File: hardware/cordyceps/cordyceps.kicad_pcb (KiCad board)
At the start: 4 copper layers, 22.1 x 29.9 mm, 23 parts, among them J1 KH-1.27PH180-2X5P-L7.2-SMT, SW1 TS-1187A-B-A-B, U1 nRF52833-QDxx, X1 32Mhz crystal, X2 32.768kHz crystal

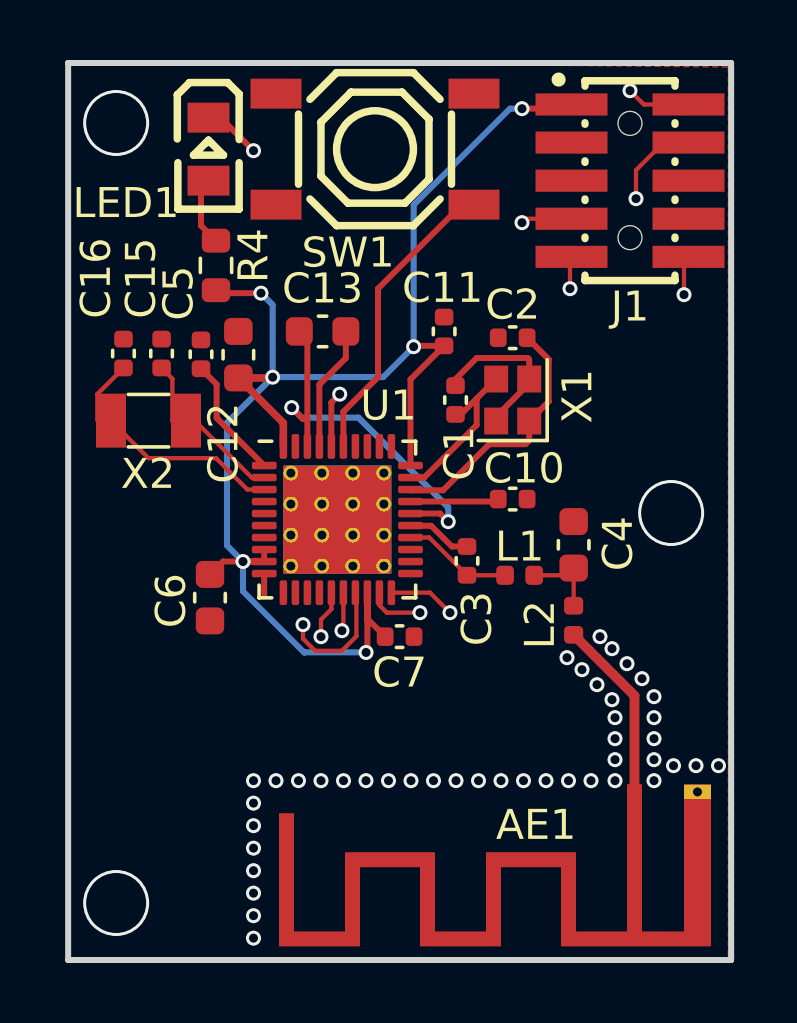
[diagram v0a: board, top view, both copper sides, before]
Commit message: Remove some redundant tracks
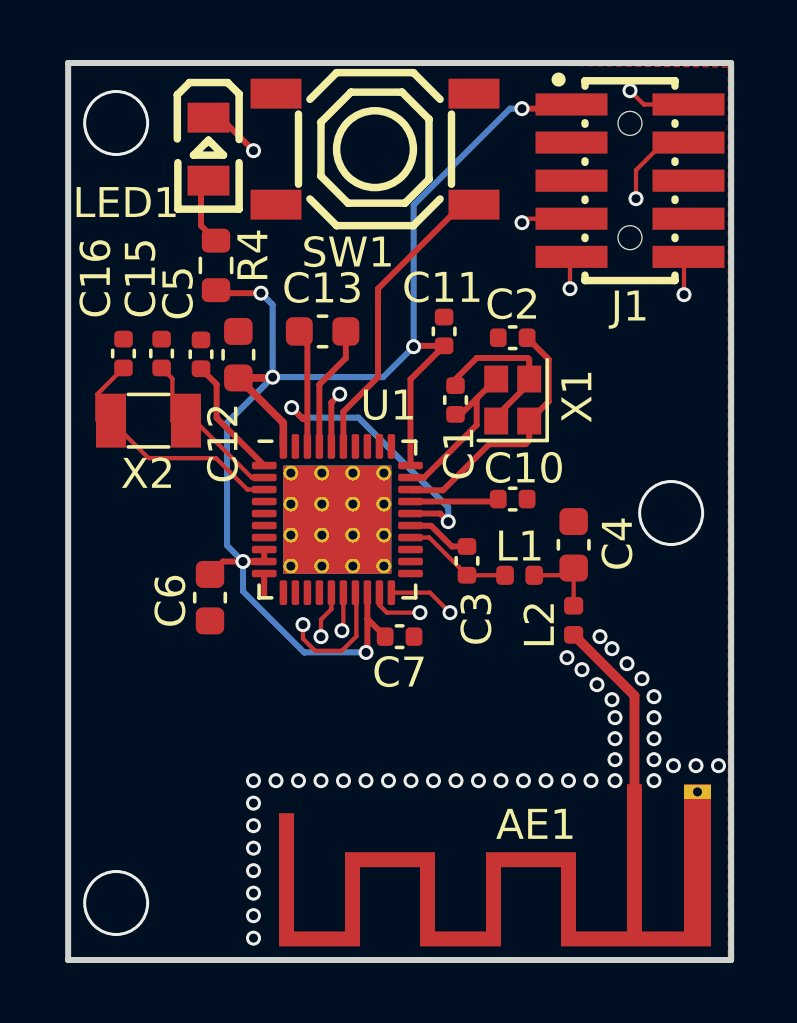
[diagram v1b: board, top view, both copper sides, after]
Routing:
- net VDD: track 51.2 -> 49.4 mm
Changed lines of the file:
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@@
-	)
-	(segment
-		(start 123.045779 90.675778)
-		(end 123.045779 89.733479)
-		(width 0.2)
-		(layer "F.Cu")
-		(net 8)
-	)
-	(segment
-		(start 123.045779 90.605779)
-		(end 123.045779 89.733479)
-		(width 0.2)
-		(layer "F.Cu")
-		(net 8)
 	)
 	(segment

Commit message: Add 2 MOSFETs to be able to turn things on and off
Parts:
- added D1: 1N5819WS, easyeda2kicad:SOD-323_L1.8-W1.3-LS2.5-RD, F.Cu at (117.8, 97.8)
- added Q1: 2N7002, Package_TO_SOT_SMD:SOT-23, F.Cu at (122.5, 93.8)
- added Q2: IRML6401, Package_TO_SOT_SMD:SOT-23, F.Cu at (118.5, 93.8)
- added R1: 10k, Resistor_SMD:R_0402_1005Metric, F.Cu at (125.5, 93.2)
- added R2: 10k, Resistor_SMD:R_0402_1005Metric, F.Cu at (125.5, 94.3)
- moved C7 1.17 mm to (125.2, 91.5)
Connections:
- U1 pad 14: unconnected-(U1-P0.15-Pad14) -> Net-(Q1-G)
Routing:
- net VDD: track 49.4 -> 61.5 mm, vias 6 -> 7
- net Net-(Q1-G): track 0.00 -> 8.00 mm
- net Net-(Q1-D): track 0.00 -> 6.22 mm
- net /V_OUT: track 0.00 -> 2.39 mm
- net GND: vias 43 -> 44

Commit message: Add required connectors
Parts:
- added J2: Rothult_Debug_Header, Connector_PinHeader_1.27mm:PinHeader_1x06_P1.27mm_Vertical, F.Cu at (114.7, 93.7)
- added J3: Conn_01x03_Pin, Connector_PinHeader_2.54mm:PinHeader_1x03_P2.54mm_Vertical, F.Cu at (133.6, 90.7)
- added R3: 10k, Resistor_SMD:R_0402_1005Metric, F.Cu at (117.8, 86.7)
- added R5: 10k, Resistor_SMD:R_0402_1005Metric, F.Cu at (116.8, 86.7)
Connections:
- net /V_OUT renamed Net-(D1-C)
- U1 pad 6: unconnected-(U1-P1.09-Pad6) -> /ROTHULT_TX
- U1 pad 7: unconnected-(U1-P0.011-Pad7) -> /ROTHULT_RX
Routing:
- net VDD: track 61.5 -> 82.7 mm, vias 7 -> 8
- net Net-(D1-C): track 2.39 -> 21.4 mm, vias 0 -> 1
- net /ROTHULT_RX: track 0.00 -> 5.76 mm
- net /ROTHULT_TX: track 0.00 -> 5.48 mm
- net GND: vias 44 -> 45
- net (no net): vias 3 -> 2
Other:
- board text added: "CLK"
- board text added: "GND"
- board text added: "IO"
- board text added: "V_IN"
- board text added: "V_OUT"

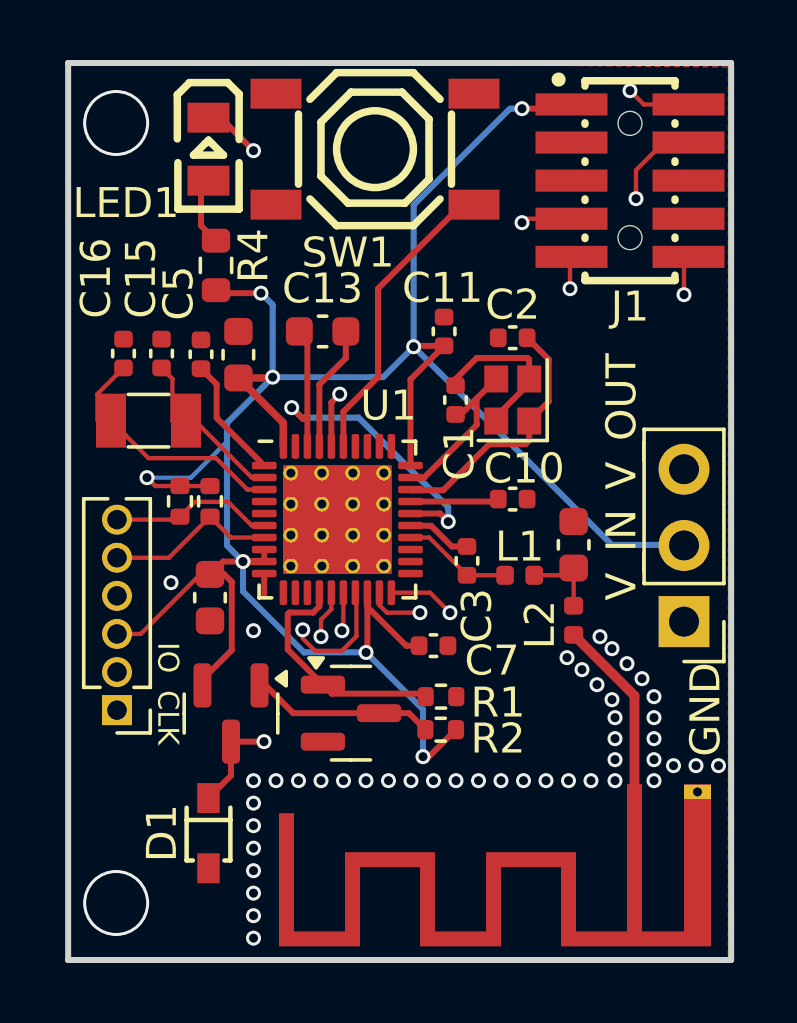
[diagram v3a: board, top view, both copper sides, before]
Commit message: Add some GND vias
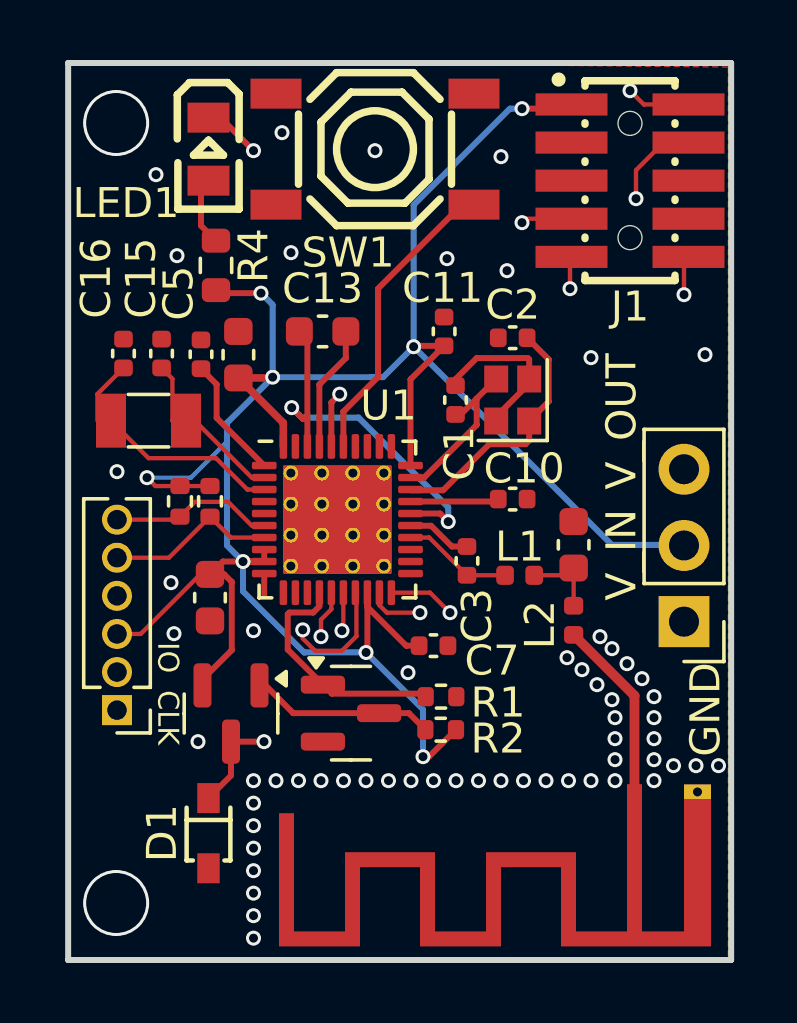
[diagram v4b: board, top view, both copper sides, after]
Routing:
- net GND: vias 45 -> 59
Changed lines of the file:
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@@
 		)
 		(property "Value" "Rothult_Debug_Header"
-			(at 0 8.045 360)
+			(at 0 8.045 0)
 			(layer "F.Fab")
 			(effects
@@
 		(tags "Through hole pin header THT 1x03 2.54mm single row")
 		(property "Reference" "J3"
-			(at 0.1 -2.5 360)
+			(at 0.1 -2.5 0)
 			(layer "F.SilkS")
 			(hide yes)
@@
 		)
 		(property "Value" "Conn_01x03_Pin"
-			(at 0 7.41 360)
+			(at 0 7.41 0)
 			(layer "F.Fab")
 			(effects
@@
 	)
 	(via
+		(at 116 75.8)
+		(size 0.5)
+		(drill 0.3)
+		(layers "F.Cu" "B.Cu")
+		(free yes)
+		(net 3)
+	)
+	(via
 		(at 129 96)
 		(size 0.5)
@@
 	)
 	(via
+		(at 127.5 75.2)
+		(size 0.5)
+		(drill 0.3)
+		(layers "F.Cu" "B.Cu")
+		(free yes)
+		(net 3)
+	)
+	(via
 		(at 131.3 96)
 		(size 0.5)
@@
 	)
 	(via
+		(at 123.3 75)
+		(size 0.5)
+		(drill 0.3)
+		(layers "F.Cu" "B.Cu")
+		(free yes)
+		(net 3)
+	)
+	(via
 		(at 123 96)
 		(size 0.5)
@@
 	)
 	(via
+		(at 134.3 81.8)
+		(size 0.5)
+		(drill 0.3)
+		(layers "F.Cu" "B.Cu")
+		(free yes)
+		(net 3)
+	)
+	(via
 		(at 125.25 96)
 		(size 0.5)
@@
 	)
 	(via
+		(at 124.4 92.4)
+		(size 0.5)
+		(drill 0.3)
+		(layers "F.Cu" "B.Cu")
+		(free yes)
+		(net 3)
+	)
+	(via
 		(at 132.6 95.3)
 		(size 0.5)
@@
 	)
 	(via
+		(at 117.4 94.7)
+		(size 0.5)
+		(drill 0.3)
+		(layers "F.Cu" "B.Cu")
+		(free yes)
+		(net 3)
+	)
+	(via
 		(at 119.25 99)
 		(size 0.5)
@@
 	)
 	(via
+		(at 120.5 78.4)
+		(size 0.5)
+		(drill 0.3)
+		(layers "F.Cu" "B.Cu")
+		(free yes)
+		(net 3)
+	)
+	(via
 		(at 134.75 95.5)
 		(size 0.5)
@@
 	)
 	(via
+		(at 114.7 85.7)
+		(size 0.5)
+		(drill 0.3)
+		(layers "F.Cu" "B.Cu")
+		(free yes)
+		(net 3)
+	)
+	(via
+		(at 120.2 74.4)
+		(size 0.5)
+		(drill 0.3)
+		(layers "F.Cu" "B.Cu")
+		(free yes)
+		(net 3)
+	)
+	(via
 		(at 132.2 92.6)
 		(size 0.5)
@@
 	)
 	(via
+		(at 116.6 91.1)
+		(size 0.5)
+		(drill 0.3)
+		(layers "F.Cu" "B.Cu")
+		(free yes)
+		(net 3)
+	)
+	(via
 		(at 131.3 95.3)
 		(size 0.5)
@@
 	)
 	(via
+		(at 127.7 79)
+		(size 0.5)
+		(drill 0.3)
+		(layers "F.Cu" "B.Cu")
+		(free yes)
+		(net 3)
+	)
+	(via
 		(at 120.75 96)
 		(size 0.5)
@@
 	)
 	(via
+		(at 130.5 81.9)
+		(size 0.5)
+		(drill 0.3)
+		(layers "F.Cu" "B.Cu")
+		(free yes)
+		(net 3)
+	)
+	(via
 		(at 130.2 92.3)
 		(size 0.5)
@@
 		(size 0.5)
 		(drill 0.3)
+		(layers "F.Cu" "B.Cu")
+		(free yes)
+		(net 3)
+	)
+	(via
+		(at 125.7 78.6)
+		(size 0.5)
+		(drill 0.3)
+		(layers "F.Cu" "B.Cu")
+		(free yes)
+		(net 3)
+	)
+	(via
+		(at 116.7 78.5)
+		(size 0.5)
+		(drill 0.3)

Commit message: Fix the small fuckup with the UART RX/TX on cordyceps board
Oops, I did it again!
Luckily, we can just reassign those as nRF chips allow to use any pin as RX/TX.
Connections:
- J1 pad 7: /DBG_TX -> /DBG_RX
- J1 pad 9: /DBG_RX -> /DBG_TX
- U1 pad 15: /DBG_RX -> /DBG_TX
- U1 pad 17: /DBG_TX -> /DBG_RX
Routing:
- net /DBG_TX: track 23.4 -> 18.8 mm
- net /DBG_RX: track 18.8 -> 23.4 mm
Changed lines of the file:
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@@
 			(layers "F.Cu" "F.Paste" "F.Mask")
 			(roundrect_rratio 0.25)
-			(net 24 "/DBG_RX")
+			(net 37 "/DBG_TX")
 			(pinfunction "P0.17")
 			(pintype "bidirectional")
@@
 			(layers "F.Cu" "F.Paste" "F.Mask")
 			(roundrect_rratio 0.25)
-			(net 37 "/DBG_TX")
+			(net 24 "/DBG_RX")
 			(pinfunction "P0.20")
 			(pintype "bidirectional")
@@
 			(size 0.74 2.4)
 			(layers "F.Cu" "F.Paste" "F.Mask")
-			(net 37 "/DBG_TX")
+			(net 24 "/DBG_RX")
 			(pinfunction "7")
 			(pintype "unspecified")
@@
 			(size 0.74 2.4)
 			(layers "F.Cu" "F.Paste" "F.Mask")
-			(net 24 "/DBG_RX")
+			(net 37 "/DBG_TX")
 			(pinfunction "9")
 			(pintype "unspecified")
@@
 	)
 	(segment
-		(start 129.8 79.6)
-		(end 129.8 78.59)
+		(start 122.195716 91.6725)
+		(end 122.68045 91.187766)
 		(width 0.145)
 		(layer "F.Cu")
@@
 	)
 	(segment
-		(start 129.8 78.59)
-		(end 129.85 78.54)
+		(start 122.68045 89.76815)
+		(end 122.645779 89.733479)
 		(width 0.145)
 		(layer "F.Cu")
@@
 	)
 	(segment
-		(start 121.5 91.2)
-		(end 121.5 90.631784)
+		(start 121.304284 91.6725)
+		(end 122.195716 91.6725)
 		(width 0.145)
 		(layer "F.Cu")
@@
 	)
 	(segment
-		(start 121.845779 90.286005)
-		(end 121.845779 89.733479)
+		(start 128.2 77.4)
+		(end 128.33 77.27)
 		(width 0.145)
 		(layer "F.Cu")
@@
 	)
 	(segment
-		(start 121.5 90.631784)
-		(end 121.845779 90.286005)
+		(start 120.89092 91.259136)
+		(end 121.304284 91.6725)
+		(width 0.145)
+		(layer "F.Cu")
+		(net 24)
+	)
+	(segment
+		(start 120.89092 90.973013)
+		(end 120.89092 91.259136)
+		(width 0.145)
+		(layer "F.Cu")
+		(net 24)
+	)
+	(segment
+		(start 128.33 77.27)
+		(end 129.85 77.27)
+		(width 0.145)
+		(layer "F.Cu")
+		(net 24)
+	)
+	(segment
+		(start 122.68045 91.187766)
+		(end 122.68045 89.76815)
 		(width 0.145)
 		(layer "F.Cu")
@@
 	)
 	(via
-		(at 121.5 91.2)
+		(at 120.89092 90.973013)
 		(size 0.5)
 		(drill 0.3)
@@
 	)
 	(via
-		(at 129.8 79.6)
+		(at 128.2 77.4)
 		(size 0.5)
 		(drill 0.3)
@@
 	)
 	(segment
-		(start 121.5 91.031784)
-		(end 122.604284 89.9275)
+		(start 120.89092 90.973013)
+		(end 120.958771 90.973013)
 		(width 0.145)
 		(layer "In2.Cu")
@@
 	)
 	(segment
-		(start 129.8 84.6)
-		(end 129.8 79.6)
+		(start 125.060279 80.539721)
+		(end 128.2 77.4)
 		(width 0.145)
 		(layer "In2.Cu")
@@
 	)
 	(segment
-		(start 124.4725 89.9275)
-		(end 129.8 84.6)
+		(start 124.2 89.6)
+		(end 125.060279 88.739721)
 		(width 0.145)
 		(layer "In2.Cu")
@@
 	)
 	(segment
-		(start 122.604284 89.9275)
-		(end 124.4725 89.9275)
+		(start 125.060279 88.739721)
+		(end 125.060279 80.539721)
 		(width 0.145)
 		(layer "In2.Cu")
@@
 	)
 	(segment
-		(start 121.5 91.2)
-		(end 121.5 91.031784)
+		(start 120.958771 90.973013)
+		(end 122.331784 89.6)
 		(width 0.145)
 		(layer "In2.Cu")
@@
 	)
 	(segment
-		(start 122.195716 91.6725)
-		(end 122.68045 91.187766)
-		(width 0.145)
-		(layer "F.Cu")
-		(net 37)
-	)
-	(segment
-		(start 122.68045 89.76815)
-		(end 122.645779 89.733479)
-		(width 0.145)
-		(layer "F.Cu")
-		(net 37)
-	)
-	(segment
-		(start 121.304284 91.6725)
-		(end 122.195716 91.6725)
+		(start 122.331784 89.6)
+		(end 124.2 89.6)
 		(width 0.145)
-		(layer "F.Cu")
-		(net 37)
+		(layer "In2.Cu")
+		(net 24)
 	)
 	(segment
-		(start 128.2 77.4)
-		(end 128.33 77.27)
+		(start 129.8 79.6)
+		(end 129.8 78.59)
 		(width 0.145)
 		(layer "F.Cu")
@@
 	)
 	(segment
-		(start 120.89092 91.259136)
-		(end 121.304284 91.6725)
+		(start 129.8 78.59)
+		(end 129.85 78.54)
 		(width 0.145)
 		(layer "F.Cu")
@@
 	)
 	(segment
-		(start 120.89092 90.973013)
-		(end 120.89092 91.259136)
+		(start 121.5 91.2)
+		(end 121.5 90.631784)
 		(width 0.145)
 		(layer "F.Cu")
@@
 	)
 	(segment
-		(start 128.33 77.27)
-		(end 129.85 77.27)
+		(start 121.845779 90.286005)
+		(end 121.845779 89.733479)
 		(width 0.145)
 		(layer "F.Cu")
@@
 	)
 	(segment
-		(start 122.68045 91.187766)
-		(end 122.68045 89.76815)
+		(start 121.5 90.631784)
+		(end 121.845779 90.286005)
 		(width 0.145)
 		(layer "F.Cu")
@@
 	)
 	(via
-		(at 120.89092 90.973013)
+		(at 121.5 91.2)
 		(size 0.5)
 		(drill 0.3)
@@
 	)
 	(via
-		(at 128.2 77.4)
+		(at 129.8 79.6)
 		(size 0.5)
 		(drill 0.3)
@@
 	)
 	(segment
-		(start 120.89092 90.973013)
-		(end 120.958771 90.973013)
-		(width 0.145)
-		(layer "In2.Cu")
-		(net 37)
-	)
-	(segment
-		(start 125.060279 80.539721)
-		(end 128.2 77.4)
+		(start 121.5 91.031784)
+		(end 122.604284 89.9275)
 		(width 0.145)
 		(layer "In2.Cu")
@@
 	)
 	(segment
-		(start 124.2 89.6)
-		(end 125.060279 88.739721)
+		(start 129.8 84.6)
+		(end 129.8 79.6)
 		(width 0.145)
 		(layer "In2.Cu")
@@
 	)
 	(segment
-		(start 125.060279 88.739721)
-		(end 125.060279 80.539721)
+		(start 124.4725 89.9275)
+		(end 129.8 84.6)
 		(width 0.145)
 		(layer "In2.Cu")
@@
 	)
 	(segment
-		(start 120.958771 90.973013)
-		(end 122.331784 89.6)
+		(start 122.604284 89.9275)
+		(end 124.4725 89.9275)
 		(width 0.145)
 		(layer "In2.Cu")
@@
 	)
 	(segment
-		(start 122.331784 89.6)
-		(end 124.2 89.6)
+		(start 121.5 91.2)
+		(end 121.5 91.031784)
 		(width 0.145)
 		(layer "In2.Cu")
